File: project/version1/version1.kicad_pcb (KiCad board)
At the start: 2 copper layers, 6 parts, among them IC1 ESP32-S3-WROOM-1-N16R2, IC2 TJA1050T_CM,118, IC3 ADS1115LIDGSR

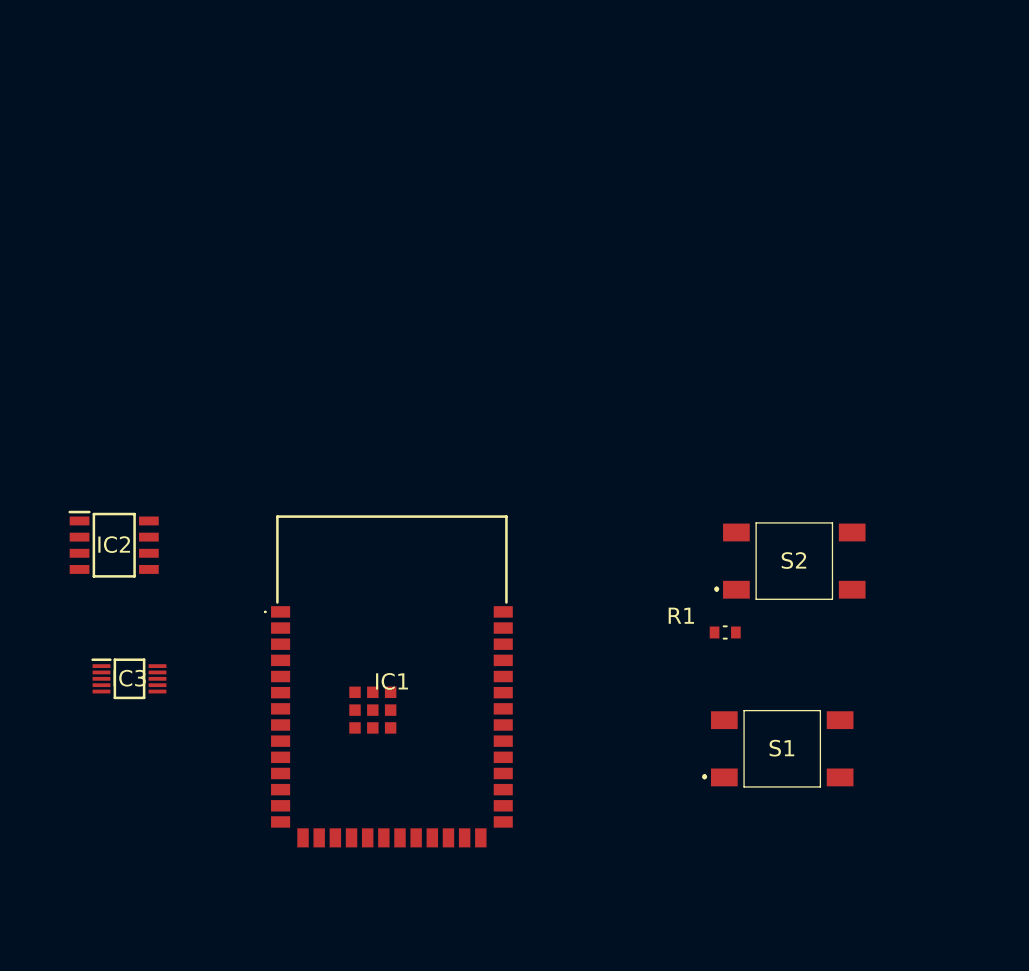
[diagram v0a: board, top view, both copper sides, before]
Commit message: placed initial components, leds, etc... Started working on routing the tracks
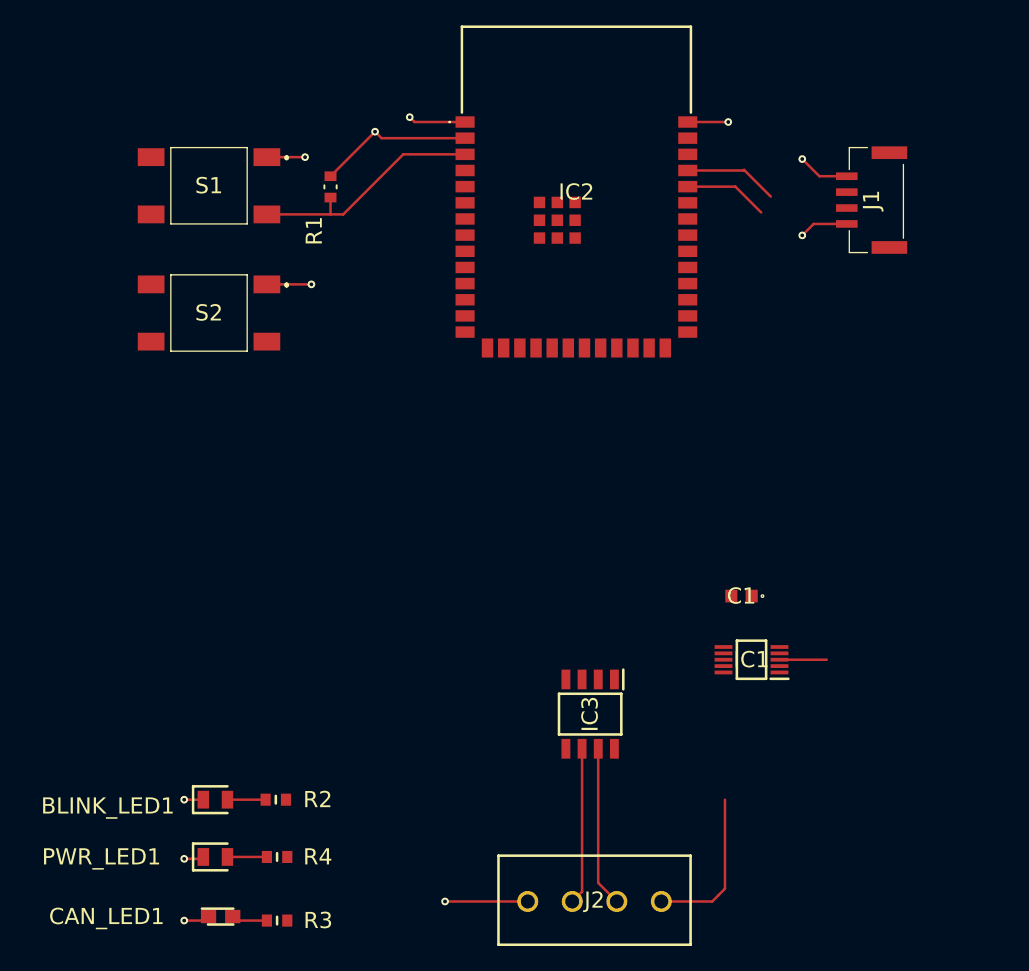
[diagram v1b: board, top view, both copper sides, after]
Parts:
- added BLINK_LED1: 150080BS75000, Library:LEDC2012X70N, F.Cu at (54.0, 65.5)
- added C1: C0603C104K5RACTU, Library:C0603, F.Cu at (95.3, 49.5)
- added CAN_LED1: 150080GS75000, Library:LEDM2012X70N, F.Cu at (54.4, 74.7)
- added J1: BM04B-GVHS-TB_LF__SN_, Library:BM04BGVHSTBLFSN, F.Cu at (105.8, 18.4)
- added J2: OSTTE040104, Library:OSTTE040104, F.Cu at (89.0, 73.5)
- added PWR_LED1: 150080RS75000, Library:LEDC2012X70N, F.Cu at (54.0, 70.0)
- added R2: RC0603FR-07220RL, Library:RESC1608X55N, F.Cu at (58.7, 65.5)
- added R3: RC0603FR-07220RL, Library:RESC1608X55N, F.Cu at (58.8, 75.0)
- added R4: RC0603FR-07220RL, Library:RESC1608X55N, F.Cu at (58.8, 70.0)
- moved S2 56.6 mm to (53.5, 27.2), turned to 180 degrees
- moved S1 54.6 mm to (53.5, 17.2), turned to 180 degrees
- moved IC1 48.9 mm to (96.1, 54.5), turned to 180 degrees
- moved R1 46.8 mm to (63.0, 17.3), turned to 90 degrees
- moved IC2 41.1 mm to (82.3, 17.5)
- moved IC3 39.7 mm to (83.4, 58.8), turned to -90 degrees
- renumbered IC3 to IC1, IC1 to IC2, IC2 to IC3, S2 to S1, S1 to S2
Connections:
- IC2 pad 28: unconnected-(IC1-IO35-Pad28) -> Net-(IC2-IO35)
- IC2 pad 29: unconnected-(IC1-IO36-Pad29) -> Net-(IC2-IO36)
- IC2 pad 3: Net-(IC1-EN) -> Net-(IC2-EN)
- IC2 pad 36: unconnected-(IC1-RXD0-Pad36) -> Net-(IC2-RXD0)
- IC2 pad 37: unconnected-(IC1-TXD0-Pad37) -> Net-(IC2-TXD0)
- IC3 pad 1: unconnected-(IC2-TXD-Pad1) -> Net-(IC2-IO35)
- IC3 pad 4: unconnected-(IC2-RXD-Pad4) -> Net-(IC2-IO36)
- IC3 pad 6: unconnected-(IC2-CANL-Pad6) -> Net-(IC3-CANL)
- IC3 pad 7: unconnected-(IC2-CANH-Pad7) -> Net-(IC3-CANH)
- R1 pad 1: Net-(IC1-EN) -> Net-(IC2-EN)
- S1 pad 1: unconnected-(S2-Pad1) -> GND
- S1 pad 2: Net-(IC1-EN) -> unconnected-(S1-Pad2)
- S1 pad 3: unconnected-(S2-Pad3) -> Net-(IC2-EN)
- S1 pad 4: GND -> unconnected-(S1-Pad4)
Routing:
- net GND: track 0.00 -> 24.8 mm, vias 0 -> 9
- net Net-(IC2-EN): track 0.00 -> 17.5 mm
- net +3.3V: track 0.00 -> 16.1 mm, vias 0 -> 2
- net Net-(IC3-CANH): track 0.00 -> 12.6 mm
- net +5V: track 0.00 -> 12.4 mm
- net Net-(IC3-CANL): track 0.00 -> 12.3 mm
- net Net-(IC2-TXD0): track 0.00 -> 7.42 mm
- net Net-(IC2-RXD0): track 0.00 -> 6.62 mm
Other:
- copper layers 2 -> 4

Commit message: added voltage regulator
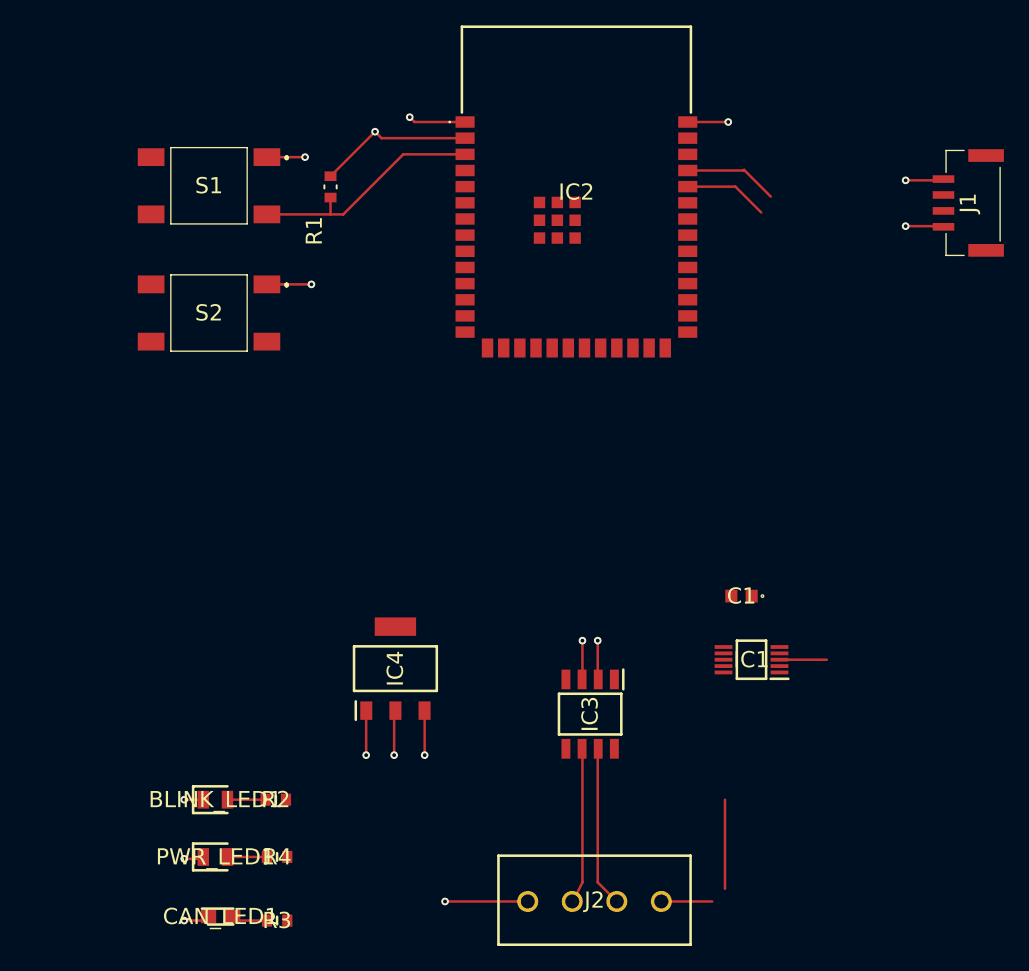
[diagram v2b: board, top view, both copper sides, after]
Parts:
- added IC4: AMS1117-3.3, Library:SOT229P700X180-4N, F.Cu at (68.1, 55.2)
- moved J1 7.60 mm to (113.4, 18.6)
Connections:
- J1 pad 1: +3.3V -> +5V
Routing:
- net Net-(IC3-CANH): track 12.6 -> 0.00 mm
- net Net-(IC3-CANL): track 12.3 -> 0.00 mm
- net GND: track 24.8 -> 20.7 mm, vias 9 -> 11
- net +3.3V: track 16.1 -> 12.2 mm, vias 2 -> 3
- net +5V: track 12.4 -> 11.0 mm, vias 0 -> 2
